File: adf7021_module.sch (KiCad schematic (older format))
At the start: 68 parts, among them J1 Conn_02x10_Counter_Clockwise, J2 Conn_Coaxial, J3 Conn_Coaxial, J4 Conn_02x10_Counter_Clockwise, U1 ADF7021, X1 19.68MHz

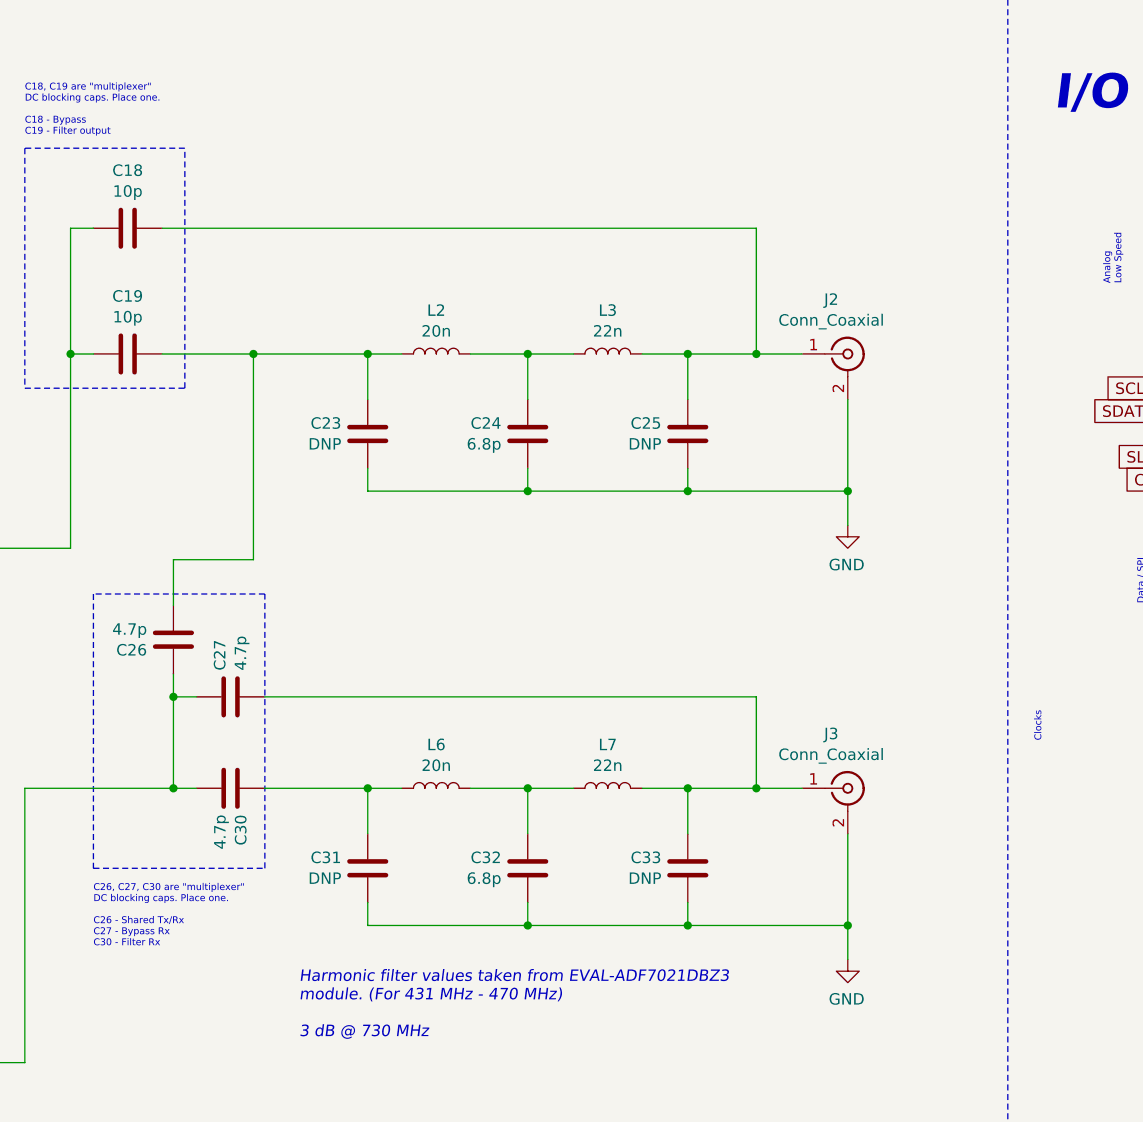
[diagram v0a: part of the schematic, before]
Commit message: RF bypass will use auxillary U.FL instead of SMA
This greatly reduces schematic complexity. Since this is more of a
"debug" feature that we do not anticipate using much, it seems ok to
make this a secondary connector.
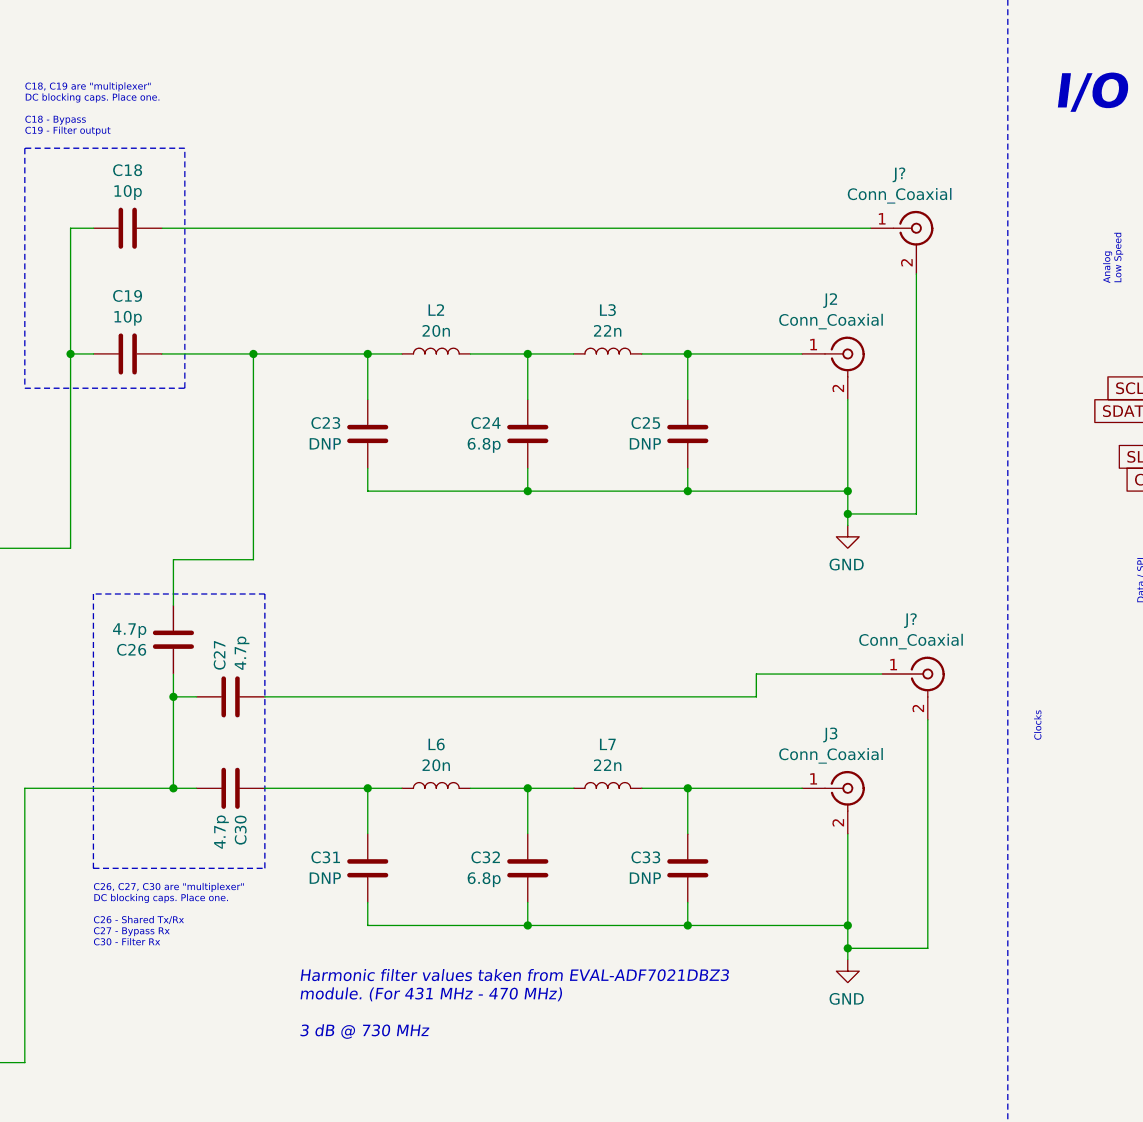
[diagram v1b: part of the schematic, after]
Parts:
- added J? (x2): Conn_Coaxial, Connector_Coaxial:U.FL_Hirose_U.FL-R-SMT-1_Vertical, symbol Connector:Conn_Coaxial
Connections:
- net GND: now also J?.2 (Ext), J?.2 (Ext)
- net at C25.1, J2.1 (In), L3.1: no longer C18.1
- net at C33.1, J3.1 (In), L7.1: no longer C27.2
- new net: C27.2, J?.1 (In)
- new net: C18.1, J?.1 (In)
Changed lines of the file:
@@
 $EndComp
 Wire Wire Line
-	9400 9700 9400 9550
+	9400 9700 9400 9650
 Wire Wire Line
 	8700 9550 8000 9550
@@
 	1    0    0    -1
 $EndComp
-Wire Wire Line
-	9200 8950 9000 8950
 Connection ~ 8700 8950
 Wire Wire Line
@@
 $EndComp
 Wire Wire Line
-	9400 7800 9400 7650
+	9400 7800 9400 7750
 Wire Wire Line
 	8700 7650 8000 7650
@@
 	1    0    0    -1
 $EndComp
-Wire Wire Line
-	9200 7050 9000 7050
 Connection ~ 8700 7050
 Wire Wire Line
@@
 Wire Wire Line
 	6850 8550 9000 8550
-Wire Wire Line
-	9000 8550 9000 8950
-Connection ~ 9000 8950
-Wire Wire Line
-	9000 8950 8700 8950
 $Comp
 L Device:C C?
@@
 	6000 6500 6100 6500
 Connection ~ 6000 7050
-Wire Wire Line
-	6400 6500 9000 6500
-Wire Wire Line
-	9000 6500 9000 7050
-Connection ~ 9000 7050
-Wire Wire Line
-	9000 7050 8700 7050
 Text Notes 6100 9650 0    30   ~ 0
 C26, C27, C30 are "multiplexer"\nDC blocking caps. Place one.\n\nC26 - Shared Tx/Rx\nC27 - Bypass Rx\nC30 - Filter Rx
@@
 	3550 7900 3850 7900
 Connection ~ 3850 7900
+$Comp
+L Connector:Conn_Coaxial J?
+U 1 1 5FEAE683
+P 9750 8450
+AR Path="/5FB73817/5FEAE683" Ref="J?"  Part="1"
+AR Path="/5FEAE683" Ref="J?"  Part="1"
+F 0 "J?" H 9678 8688 50  0000 C CNN
+F 1 "Conn_Coaxial" H 9678 8597 50  0000 C CNN
+F 2 "Connector_Coaxial:U.FL_Hirose_U.FL-R-SMT-1_Vertical" H 9750 8450 50  0001 C CNN
+F 3 " ~" H 9750 8450 50  0001 C CNN
+	1    9750 8450
+	1    0    0    -1
+$EndComp
+Wire Wire Line
+	8700 8950 9200 8950
+Wire Wire Line
+	9550 8450 9000 8450
+Wire Wire Line
+	9000 8450 9000 8550
+Wire Wire Line
+	9750 8650 9750 9650
+Wire Wire Line
+	9750 9650 9400 9650
+Connection ~ 9400 9650
+Wire Wire Line
+	9400 9650 9400 9550
+$Comp
+L Connector:Conn_Coaxial J?
+U 1 1 5FEE7F8C
+P 9700 6500
+AR Path="/5FB73817/5FEE7F8C" Ref="J?"  Part="1"
+AR Path="/5FEE7F8C" Ref="J?"  Part="1"
+F 0 "J?" H 9628 6738 50  0000 C CNN
+F 1 "Conn_Coaxial" H 9628 6647 50  0000 C CNN
+F 2 "Connector_Coaxial:U.FL_Hirose_U.FL-R-SMT-1_Vertical" H 9700 6500 50  0001 C CNN
+F 3 " ~" H 9700 6500 50  0001 C CNN
+	1    9700 6500
+	1    0    0    -1
+$EndComp
+Wire Wire Line
+	9400 7750 9700 7750
+Wire Wire Line
+	9700 7750 9700 6700
+Connection ~ 9400 7750
+Wire Wire Line
+	9400 7750 9400 7650
+Wire Wire Line
+	8700 7050 9200 7050
+Wire Wire Line
+	6400 6500 9500 6500
 $EndSCHEMATC

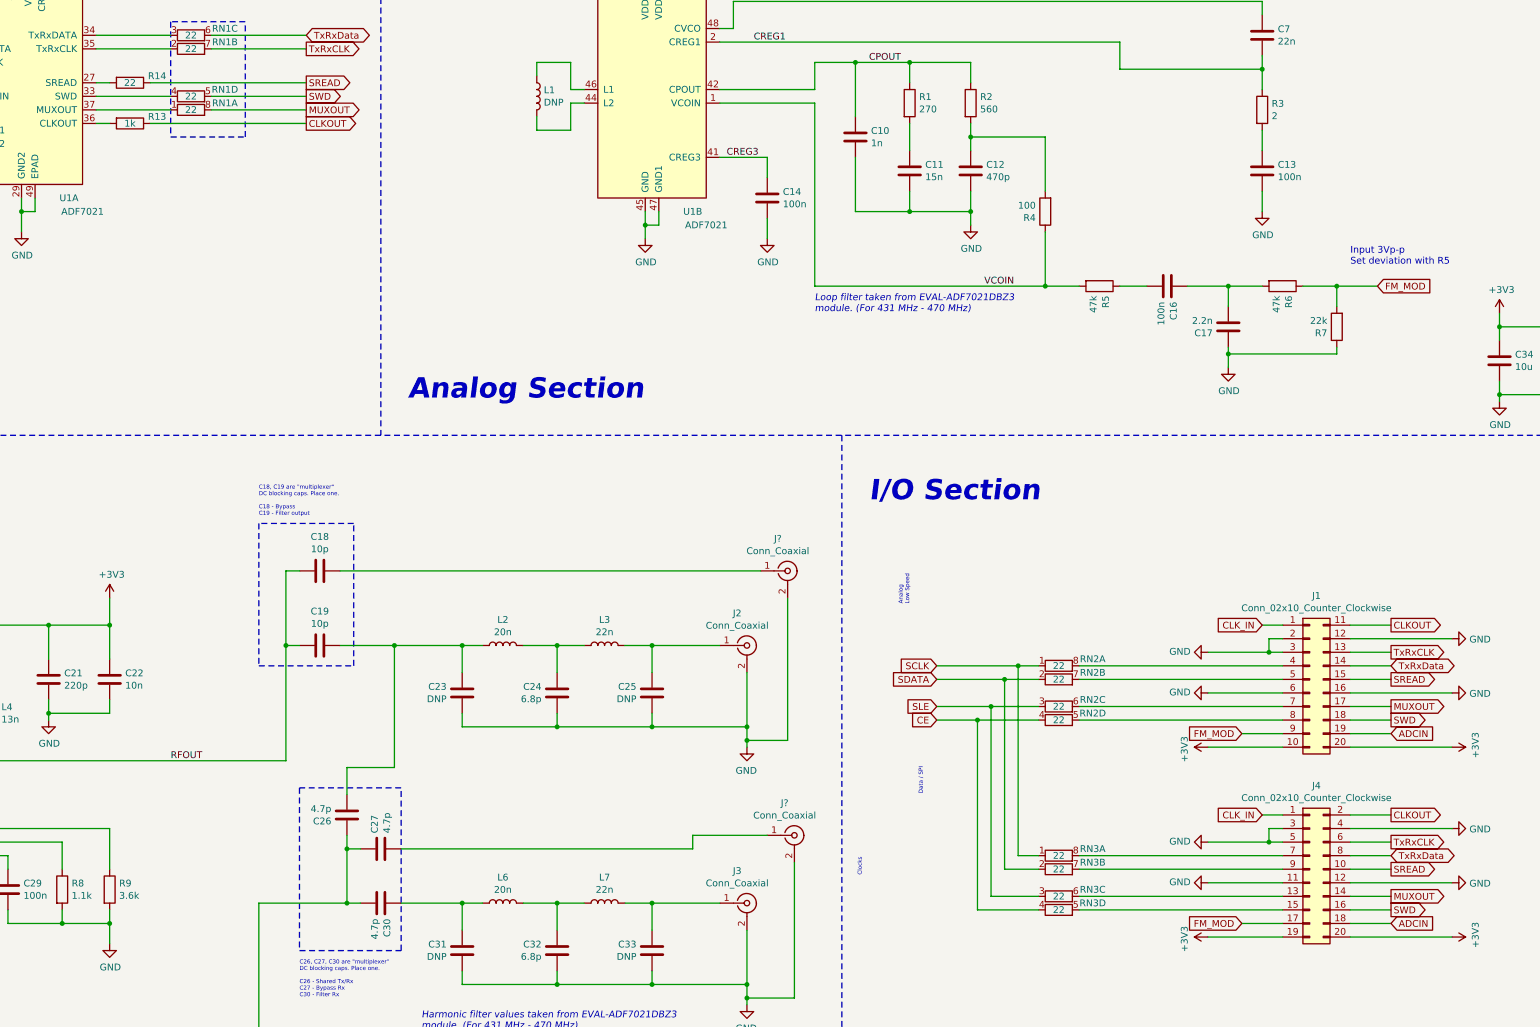
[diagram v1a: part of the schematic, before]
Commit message: Swapping ADCIN and SWD for routing sanity
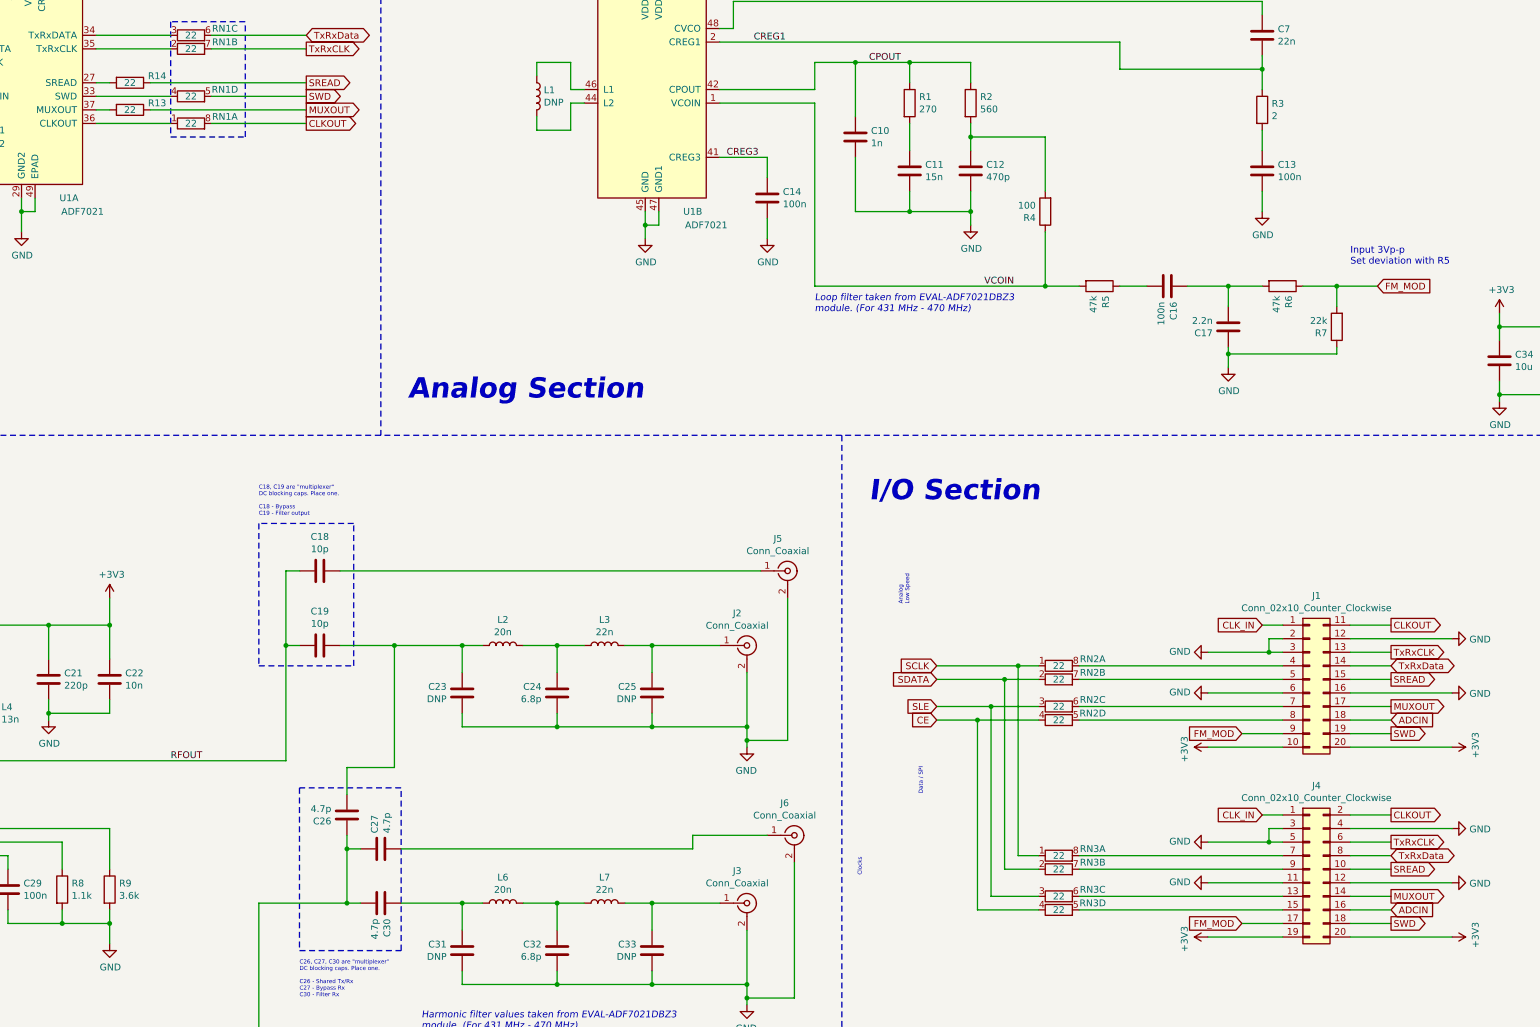
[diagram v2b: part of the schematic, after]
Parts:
- R13: value 1k -> 22
- gave numbers to parts that had none: 2
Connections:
- net ADCIN: now also J1.18 (Pin_18), J4.16 (Pin_16); no longer J1.19 (Pin_19), J4.18 (Pin_18)
- net CLKOUT: now also RN1.8 (R1.2); no longer R13.1
- net MUXOUT: now also R13.1; no longer RN1.8 (R1.2)
- net SWD: now also J1.19 (Pin_19), J4.18 (Pin_18); no longer J1.18 (Pin_18), J4.16 (Pin_16)
- net at RN1.1 (R1.1): now also U1.36 (CLKOUT); no longer U1.37 (MUXOUT)
- net at R13.2: now also U1.37 (MUXOUT); no longer U1.36 (CLKOUT)
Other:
- moved on the sheet: R13, RN1A
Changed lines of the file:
@@
 CLKOUT
 Wire Wire Line
-	4600 3100 5150 3100
+	4600 3100 4700 3100
 Wire Wire Line
 	3450 3350 3600 3350
@@
 Wire Wire Line
 	14000 1550 14400 1550
-Wire Wire Line
-	5450 3100 6150 3100
 $Comp
 L Oscillator:DFA-S2 X?
@@
 L Device:R_Pack04_Split RN1
 U 1 1 5FDA405B
-P 5300 3100
-F 0 "RN1" V 5250 3350 50  0000 C CNN
-F 1 "22" V 5300 3100 50  0000 C CNN
-F 2 "Resistor_SMD:R_Array_Concave_4x0402" V 5575 3100 50  0001 C CNN
-F 3 "~" H 5300 3100 50  0001 C CNN
-	1    5300 3100
+P 5300 3200
+F 0 "RN1" V 5250 3450 50  0000 C CNN
+F 1 "22" V 5300 3200 50  0000 C CNN
+F 2 "Resistor_SMD:R_Array_Concave_4x0402" V 5575 3200 50  0001 C CNN
+F 3 "~" H 5300 3200 50  0001 C CNN
+	1    5300 3200
 	0    1    1    0
 $EndComp
@@
 L Device:R R13
 U 1 1 606926F1
-P 4850 3200
-F 0 "R13" V 4800 3400 50  0000 C CNN
-F 1 "1k" V 4850 3200 50  0000 C CNN
-F 2 "Resistor_SMD:R_0402_1005Metric_Pad0.72x0.64mm_HandSolder" V 4780 3200 50  0001 C CNN
-F 3 "~" H 4850 3200 50  0001 C CNN
-	1    4850 3200
+P 4850 3100
+F 0 "R13" V 4800 3300 50  0000 C CNN
+F 1 "22" V 4850 3100 50  0000 C CNN
+F 2 "Resistor_SMD:R_0402_1005Metric_Pad0.72x0.64mm_HandSolder" V 4780 3100 50  0001 C CNN
+F 3 "~" H 4850 3100 50  0001 C CNN
+	1    4850 3100
 	0    1    1    0
 $EndComp
@@
 	5700 2450 5150 2450
 Wire Wire Line
-	4700 3200 4600 3200
-Wire Wire Line
 	4600 3000 5150 3000
-Wire Wire Line
-	5000 3200 6150 3200
 $Comp
 L Connector_Generic:Conn_02x10_Top_Bottom J1
@@
 	1    0    0    -1
 $EndComp
-Text GLabel 14150 7700 2    50   Input ~ 0
+Text GLabel 14150 7600 2    50   Input ~ 0
 ADCIN
 Text GLabel 14150 7200 2    50   BiDi ~ 0
@@
 Text GLabel 14150 7300 2    50   Output ~ 0
 SREAD
-Text GLabel 14150 7600 2    50   Output ~ 0
+Text GLabel 14150 7700 2    50   Output ~ 0
 SWD
 Text GLabel 14150 7500 2    50   Output ~ 0
@@
 Wire Wire Line
 	11850 8600 13350 8600
-Text GLabel 14150 9100 2    50   Input ~ 0
+Text GLabel 14150 9000 2    50   Input ~ 0
 ADCIN
 Text GLabel 14150 8600 2    50   BiDi ~ 0
@@
 Text GLabel 14150 8700 2    50   Output ~ 0
 SREAD
-Text GLabel 14150 9000 2    50   Output ~ 0
+Text GLabel 14150 9100 2    50   Output ~ 0
 SWD
 Text GLabel 14150 8900 2    50   Output ~ 0
@@
 P 9750 8450
 AR Path="/5FB73817/5FEAE683" Ref="J?"  Part="1"
-AR Path="/5FEAE683" Ref="J?"  Part="1"
-F 0 "J?" H 9678 8688 50  0000 C CNN
+AR Path="/5FEAE683" Ref="J6"  Part="1"
+F 0 "J6" H 9678 8688 50  0000 C CNN
 F 1 "Conn_Coaxial" H 9678 8597 50  0000 C CNN
 F 2 "Connector_Coaxial:U.FL_Hirose_U.FL-R-SMT-1_Vertical" H 9750 8450 50  0001 C CNN
@@
 P 9700 6500
 AR Path="/5FB73817/5FEE7F8C" Ref="J?"  Part="1"
-AR Path="/5FEE7F8C" Ref="J?"  Part="1"
-F 0 "J?" H 9628 6738 50  0000 C CNN
+AR Path="/5FEE7F8C" Ref="J5"  Part="1"
+F 0 "J5" H 9628 6738 50  0000 C CNN
 F 1 "Conn_Coaxial" H 9628 6647 50  0000 C CNN
 F 2 "Connector_Coaxial:U.FL_Hirose_U.FL-R-SMT-1_Vertical" H 9700 6500 50  0001 C CNN
@@
 Wire Wire Line
 	6400 6500 9500 6500
+Wire Wire Line
+	5450 3200 6150 3200
+Wire Wire Line
+	5000 3100 6150 3100
+Wire Wire Line
+	4600 3200 5150 3200
 $EndSCHEMATC

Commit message: adding shield, moving uFL debug connectors, adding optional SMA clock source input
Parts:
- removed H4: MountingHole_Pad, MountingHole:MountingHole_2.2mm_M2_Pad_TopBottom, symbol Mechanical:MountingHole_Pad
- added J7: RFShield_OnePiece, RF_Shielding:Laird_Technologies_BMI-S-205-F_38.10x25.40mm, symbol Device:RFShield_OnePiece
- added R11: 0, Resistor_SMD:R_0402_1005Metric_Pad0.72x0.64mm_HandSolder, symbol Device:R
- added R12, R15: DNP, Resistor_SMD:R_0402_1005Metric_Pad0.72x0.64mm_HandSolder, symbol Device:R
- X1: footprint Oscillator:Oscillator_SMD_Fordahl_DFAS2-4Pin_7.3x5.1mm -> Oscillator:Oscillator_SMD_EuroQuartz_XO32-4Pin_3.2x2.5mm_HandSoldering
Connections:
- net CLK_IN: now also R11.2; no longer C15.1, R10.2
- net GND: now also J7.1 (Shield)
- net RFIN: no longer C26.1
- net RFOUT: now also C26.1
- net at C25.1, J2.1 (In), L3.1: now also R15.1
- net at C19.1, C23.1, L2.2: no longer C26.2
- net at C30.1, C31.1, L6.2: now also C26.2
- new net: C15.1, R10.2, R11.1, R12.2
- new net CLK_SMA: R12.1, R15.2
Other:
- note added: "RX/CLKREF SMA"
- note added: "TX / RX SMA"
- note removed: "Analog\nLow Speed"
- note removed: "Clocks"
- note removed: "Data / SPI"
- moved on the sheet: C1, C15, C18, C19, C21, C22, C23, C24, C25, C26, C27, C30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

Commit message: adding VFO pin
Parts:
- added R16: DNP, Resistor_SMD:R_0402_1005Metric_Pad0.72x0.64mm_HandSolder, symbol Device:R
- added R17: 0R, Resistor_SMD:R_0402_1005Metric_Pad0.72x0.64mm_HandSolder, symbol Device:R
- J1: value Conn_02x10_Counter_Clockwise -> Conn_Board2Board
- J4: value Conn_02x10_Counter_Clockwise -> Conn_goldpin
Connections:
- net +3V3: now also J1.2 (Pin_2), J4.3 (Pin_3); no longer J1.10 (Pin_10), J4.19 (Pin_19)
- net GND: now also R17.1; no longer J1.2 (Pin_2), J4.3 (Pin_3), X1.1 (Vctrl)
- new net: R16.1, R17.2, X1.1 (Vctrl)
- new net VCO_MOD: J1.10 (Pin_10), J4.19 (Pin_19), R16.2
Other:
- note added: "Careful - pin numbers differ\nbetwen connectors"
- moved on the sheet: C1, C10, C11, C12, C13, C14, C15, C16, C17, C2, C3, C4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
